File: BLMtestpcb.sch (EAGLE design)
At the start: 92 parts, among them IC1 NTB0102DP, IC10 PIC16F18325-I/P, IC11 MAX11644EUA+, IC4 PIC24F16KA301-I/SS,, IC5 NE555D, IC6 MULTIPLEX1, IC7 AD623R, IC8 AD822R, IC9 AD623R, Q3 12MHz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

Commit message: Update to V1.1
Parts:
- JP1: value Distance Select 0B -> Type select 0
- JP2: value Type Select 0 -> Setup select 0
- JP4: value Distance Select 0A -> Type select 0
- JP5: value Type Select 1 -> Setup select 1
- JP6: value Distance Select 1A -> Type select 1
- JP9: value Distance Select 1B -> Type select 1
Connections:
- net 0A_CLOSE renamed TYPE00A
- net 0B_FAR renamed TYPE01B
- net 1A_FAR renamed TYPE10A
- net 1B_FAR renamed TYPE11B
- net BPW34_2 renamed BOT1
- net N$1 renamed OP-AMP1
- net N$35 renamed OP-AMP0
- net SFH_2700 renamed TOP0
- removed net 0A_FAR: JP4.1, PHDA2.A
- removed net 0B_CLOSE: JP1.3, PHDB1.A
- removed net 1A_CLOSE: JP6.1, PHDA3.A
- removed net 1B_CLOSE: JP9.3, PHDB4.A
- removed net BPW34: JP2.3, JP4.2
- removed net SFH_2700_2: JP5.1, JP9.2
- new net BOT0: JP2.3, JP9.2
- new net TOP1: JP4.2, JP5.1
- new net TYPE00B: JP4.1, PHDB1.A
- new net TYPE01A: JP1.3, PHDA2.A
- new net TYPE10B: JP6.1, PHDB4.A
- new net TYPE11A: JP9.3, PHDA3.A
- net +3.3V: now also IC1.OE
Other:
- moved on the sheet: JP1, JP4, JP6, JP9, PHDA1, PHDA2, PHDA3, PHDA4, PHDB1, PHDB2, PHDB3, PHDB4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

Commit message: Update to v1.2
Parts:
- JP1, JP4: value Type select 0 -> Diode select 0
- JP13: value ADC select 0 -> ADC select
- JP14: value ADC select 1 -> ADC select
- JP2: value Setup select 0 -> Setup select
- JP20: value LED Select A -> LED Select 940
- JP21: value LED Select B -> LED Select 850
- JP22: value LED Select C -> LED Select 660
- JP5: value Setup select 1 -> Setup select
- JP6, JP9: value Type select 1 -> Diode select 1
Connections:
- net N$27 renamed 940A
- net N$28 renamed 940B
- net N$29 renamed 850A
- net N$30 renamed 850B
- net N$31 renamed 660A
- net N$32 renamed 660B
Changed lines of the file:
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@@
 <part name="R8" library="rcl" library_urn="urn:adsk.eagle:library:334" deviceset="R-EU_" device="0207/10" package3d_urn="urn:adsk.eagle:package:23491/2" value="180"/>
 <part name="R9" library="resistor" library_urn="urn:adsk.eagle:library:348" deviceset="R-EU_" device="0207/10" package3d_urn="urn:adsk.eagle:package:23491/2" value="150"/>
-<part name="JP20" library="pinhead" library_urn="urn:adsk.eagle:library:325" deviceset="PINHD-1X3" device="" package3d_urn="urn:adsk.eagle:package:22458/2" value="LED Select A"/>
-<part name="JP21" library="pinhead" library_urn="urn:adsk.eagle:library:325" deviceset="PINHD-1X3" device="" package3d_urn="urn:adsk.eagle:package:22458/2" value="LED Select B"/>
-<part name="JP22" library="pinhead" library_urn="urn:adsk.eagle:library:325" deviceset="PINHD-1X3" device="" package3d_urn="urn:adsk.eagle:package:22458/2" value="LED Select C"/>
+<part name="JP20" library="pinhead" library_urn="urn:adsk.eagle:library:325" deviceset="PINHD-1X3" device="" package3d_urn="urn:adsk.eagle:package:22458/2" value="LED Select 940"/>
+<part name="JP21" library="pinhead" library_urn="urn:adsk.eagle:library:325" deviceset="PINHD-1X3" device="" package3d_urn="urn:adsk.eagle:package:22458/2" value="LED Select 850"/>
+<part name="JP22" library="pinhead" library_urn="urn:adsk.eagle:library:325" deviceset="PINHD-1X3" device="" package3d_urn="urn:adsk.eagle:package:22458/2" value="LED Select 660"/>
 <part name="JP19" library="pinhead" library_urn="urn:adsk.eagle:library:325" deviceset="PINHD-1X3" device="" package3d_urn="urn:adsk.eagle:package:22458/2" value="Pwm Select"/>
 <part name="IC7" library="analog-devices" library_urn="urn:adsk.eagle:library:102" deviceset="AD623" device="R" package3d_urn="urn:adsk.eagle:package:30987/2"/>
@@
 <part name="GND" library="supply1" library_urn="urn:adsk.eagle:library:371" deviceset="GND" device=""/>
 <part name="JP12" library="pinhead" library_urn="urn:adsk.eagle:library:325" deviceset="PINHD-1X3" device="" package3d_urn="urn:adsk.eagle:package:22458/2" value="PWM Select"/>
-<part name="JP13" library="pinhead" library_urn="urn:adsk.eagle:library:325" deviceset="PINHD-1X3" device="" package3d_urn="urn:adsk.eagle:package:22458/2" value="ADC select 0"/>
-<part name="JP14" library="pinhead" library_urn="urn:adsk.eagle:library:325" deviceset="PINHD-1X3" device="" package3d_urn="urn:adsk.eagle:package:22458/2" value="ADC select 1"/>
+<part name="JP13" library="pinhead" library_urn="urn:adsk.eagle:library:325" deviceset="PINHD-1X3" device="" package3d_urn="urn:adsk.eagle:package:22458/2" value="ADC select"/>
+<part name="JP14" library="pinhead" library_urn="urn:adsk.eagle:library:325" deviceset="PINHD-1X3" device="" package3d_urn="urn:adsk.eagle:package:22458/2" value="ADC select"/>
 <part name="JP15" library="pinhead" library_urn="urn:adsk.eagle:library:325" deviceset="PINHD-1X3" device="" package3d_urn="urn:adsk.eagle:package:22458/2" value="MCU Select"/>
 <part name="JP16" library="pinhead" library_urn="urn:adsk.eagle:library:325" deviceset="PINHD-1X3" device="" package3d_urn="urn:adsk.eagle:package:22458/2" value="MCU Select"/>
@@
 <part name="PHDB4" library="adafruit" deviceset="DIODE" device="_SOD-123FL" value="SFH 2700"/>
 <part name="PHDA4" library="adafruit" deviceset="DIODE" device="SOT23_WAVE" value="BPW34"/>
-<part name="JP4" library="pinhead" library_urn="urn:adsk.eagle:library:325" deviceset="PINHD-1X3" device="" package3d_urn="urn:adsk.eagle:package:22458/2" value="Type select 0"/>
-<part name="JP1" library="pinhead" library_urn="urn:adsk.eagle:library:325" deviceset="PINHD-1X3" device="" package3d_urn="urn:adsk.eagle:package:22458/2" value="Type select 0"/>
-<part name="JP2" library="pinhead" library_urn="urn:adsk.eagle:library:325" deviceset="PINHD-1X3" device="" package3d_urn="urn:adsk.eagle:package:22458/2" value="Setup select 0"/>
-<part name="JP5" library="pinhead" library_urn="urn:adsk.eagle:library:325" deviceset="PINHD-1X3" device="" package3d_urn="urn:adsk.eagle:package:22458/2" value="Setup select 1"/>
-<part name="JP6" library="pinhead" library_urn="urn:adsk.eagle:library:325" deviceset="PINHD-1X3" device="" package3d_urn="urn:adsk.eagle:package:22458/2" value="Type select 1"/>
-<part name="JP9" library="pinhead" library_urn="urn:adsk.eagle:library:325" deviceset="PINHD-1X3" device="" package3d_urn="urn:adsk.eagle:package:22458/2" value="Type select 1"/>
+<part name="JP4" library="pinhead" library_urn="urn:adsk.eagle:library:325" deviceset="PINHD-1X3" device="" package3d_urn="urn:adsk.eagle:package:22458/2" value="Diode select 0"/>
+<part name="JP1" library="pinhead" library_urn="urn:adsk.eagle:library:325" deviceset="PINHD-1X3" device="" package3d_urn="urn:adsk.eagle:package:22458/2" value="Diode select 0"/>
+<part name="JP2" library="pinhead" library_urn="urn:adsk.eagle:library:325" deviceset="PINHD-1X3" device="" package3d_urn="urn:adsk.eagle:package:22458/2" value="Setup select"/>
+<part name="JP5" library="pinhead" library_urn="urn:adsk.eagle:library:325" deviceset="PINHD-1X3" device="" package3d_urn="urn:adsk.eagle:package:22458/2" value="Setup select"/>
+<part name="JP6" library="pinhead" library_urn="urn:adsk.eagle:library:325" deviceset="PINHD-1X3" device="" package3d_urn="urn:adsk.eagle:package:22458/2" value="Diode select 1"/>
+<part name="JP9" library="pinhead" library_urn="urn:adsk.eagle:library:325" deviceset="PINHD-1X3" device="" package3d_urn="urn:adsk.eagle:package:22458/2" value="Diode select 1"/>
 <part name="JP10" library="pinhead" library_urn="urn:adsk.eagle:library:325" deviceset="PINHD-1X6" device="" package3d_urn="urn:adsk.eagle:package:22472/2" value="PIC24F16 header"/>
 <part name="JP17" library="pinhead" library_urn="urn:adsk.eagle:library:325" deviceset="PINHD-1X6" device="" package3d_urn="urn:adsk.eagle:package:22472/2" value="PIC16F18 header"/>
@@
 </segment>
 </net>
-<net name="N$27" class="0">
+<net name="940A" class="0">
 <segment>
 <pinref part="R4" gate="G$1" pin="2"/>
@@
 </segment>
 </net>
-<net name="N$28" class="0">
+<net name="940B" class="0">
 <segment>
 <pinref part="JP20" gate="A" pin="1"/>
@@
 </segment>
 </net>
-<net name="N$29" class="0">
+<net name="850A" class="0">
 <segment>
 <pinref part="R5" gate="G$1" pin="2"/>
@@
 </segment>
 </net>
-<net name="N$30" class="0">
+<net name="850B" class="0">
 <segment>
 <pinref part="JP21" gate="A" pin="1"/>
@@
 </segment>
 </net>
-<net name="N$31" class="0">
+<net name="660A" class="0">
 <segment>
 <pinref part="R6" gate="G$1" pin="2"/>
@@
 </segment>
 </net>
-<net name="N$32" class="0">
+<net name="660B" class="0">
 <segment>
 <pinref part="JP22" gate="A" pin="1"/>

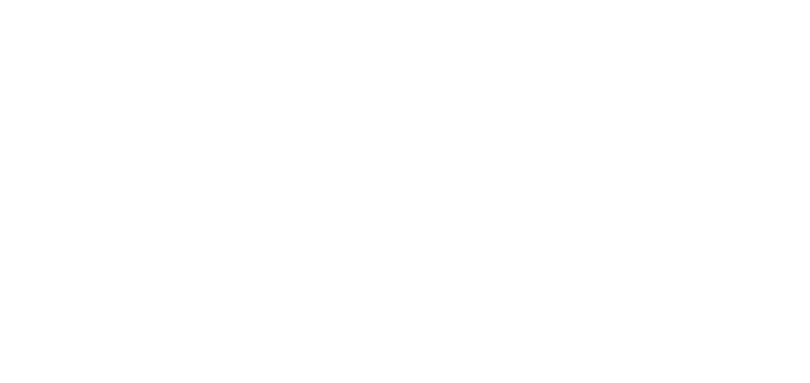
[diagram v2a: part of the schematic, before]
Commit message: Update to v1_3
Change some component footprints to have pin 1 indication. Remove 1mm length difference in PCB
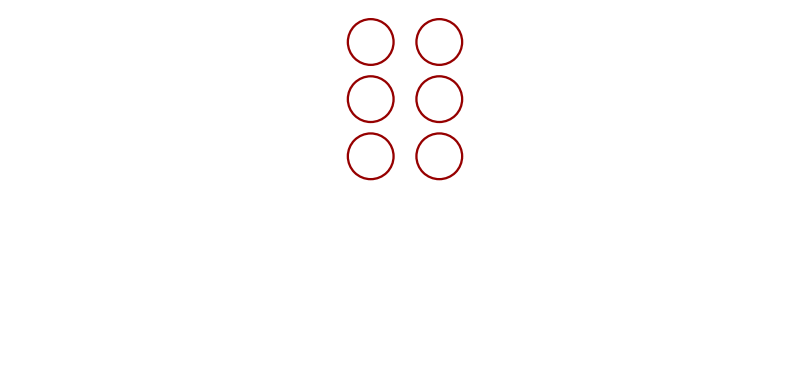
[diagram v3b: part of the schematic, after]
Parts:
- added U$1, U$2, U$3, U$4, U$5, U$6: FIDUCIAL, adafruit:FIDUCIAL
- IC5: device linear:NE555D -> linear_custom:NE555D
- IC7, IC9: device analog-devices:AD623R -> analog-devices_custom:AD623R
- IC8: device analog-devices:AD822R -> analog-devices_custom:AD822R
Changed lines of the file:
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@@
 <?xml version="1.0" encoding="utf-8"?>
 <!DOCTYPE eagle SYSTEM "eagle.dtd">
-<eagle version="9.5.1">
+<eagle version="9.4.2">
 <drawing>
 <settings>
@@
 </classes>
 <parts>
-<part name="IC5" library="linear" library_urn="urn:adsk.eagle:library:262" deviceset="*555" device="D" package3d_urn="urn:adsk.eagle:package:16404/2" technology="NE"/>
+<part name="IC5" library="linear_custom" deviceset="*555" device="D" package3d_urn="urn:adsk.eagle:package:16404/2" technology="NE"/>
 <part name="IC6" library="Peerke" deviceset="MULTIPLEX1" device=""/>
 <part name="LED1" library="adafruit" deviceset="LED" device="CHIPLED_1206" value="1328301"/>
@@
 <part name="JP22" library="pinhead" library_urn="urn:adsk.eagle:library:325" deviceset="PINHD-1X3" device="" package3d_urn="urn:adsk.eagle:package:22458/2" value="LED Select 660"/>
 <part name="JP19" library="pinhead" library_urn="urn:adsk.eagle:library:325" deviceset="PINHD-1X3" device="" package3d_urn="urn:adsk.eagle:package:22458/2" value="Pwm Select"/>
-<part name="IC7" library="analog-devices" library_urn="urn:adsk.eagle:library:102" deviceset="AD623" device="R" package3d_urn="urn:adsk.eagle:package:30987/2"/>
-<part name="IC8" library="analog-devices" library_urn="urn:adsk.eagle:library:102" deviceset="AD822" device="R" package3d_urn="urn:adsk.eagle:package:30987/2"/>
+<part name="IC7" library="analog-devices_custom" deviceset="AD623" device="R" package3d_urn="urn:adsk.eagle:package:30987/2"/>
+<part name="IC8" library="analog-devices_custom" deviceset="AD822" device="R" package3d_urn="urn:adsk.eagle:package:30987/2"/>
 <part name="GND7" library="supply1" deviceset="GND" device=""/>
 <part name="GND8" library="supply1" deviceset="GND" device=""/>
@@
 <part name="GND12" library="supply1" deviceset="GND" device=""/>
 <part name="POTMETER2" library="pot" library_urn="urn:adsk.eagle:library:331" deviceset="TRIM_EU-" device="PT10" package3d_urn="urn:adsk.eagle:package:22715/1" value="10k-100k"/>
-<part name="IC9" library="analog-devices" library_urn="urn:adsk.eagle:library:102" deviceset="AD623" device="R" package3d_urn="urn:adsk.eagle:package:30987/2"/>
+<part name="IC9" library="analog-devices_custom" deviceset="AD623" device="R" package3d_urn="urn:adsk.eagle:package:30987/2"/>
 <part name="R13" library="rcl" library_urn="urn:adsk.eagle:library:334" deviceset="R-EU_" device="0207/10" value="100k"/>
 <part name="R14" library="rcl" library_urn="urn:adsk.eagle:library:334" deviceset="R-EU_" device="0207/10" package3d_urn="urn:adsk.eagle:package:23491/2" value="1M"/>
@@
 <part name="GND15" library="supply1" library_urn="urn:adsk.eagle:library:371" deviceset="GND" device=""/>
 <part name="C16" library="rcl" library_urn="urn:adsk.eagle:library:334" deviceset="C-EU" device="025-024X044" package3d_urn="urn:adsk.eagle:package:23630/1" value="100n"/>
+<part name="U$1" library="adafruit" deviceset="FIDUCIAL" device=""/>
+<part name="U$2" library="adafruit" deviceset="FIDUCIAL" device=""/>
+<part name="U$3" library="adafruit" deviceset="FIDUCIAL" device=""/>
+<part name="U$4" library="adafruit" deviceset="FIDUCIAL" device=""/>
+<part name="U$5" library="adafruit" deviceset="FIDUCIAL" device=""/>
+<part name="U$6" library="adafruit" deviceset="FIDUCIAL" device=""/>
 </parts>
 <sheets>
@@
 <attribute name="VALUE" x="340.614" y="56.261" size="1.778" layer="96"/>
 </instance>
+<instance part="U$1" gate="G$1" x="113.03" y="172.72" smashed="yes"/>
+<instance part="U$2" gate="G$1" x="113.03" y="166.37" smashed="yes"/>
+<instance part="U$3" gate="G$1" x="113.03" y="160.02" smashed="yes"/>
+<instance part="U$4" gate="G$1" x="120.65" y="172.72" smashed="yes"/>
+<instance part="U$5" gate="G$1" x="120.65" y="166.37" smashed="yes"/>
+<instance part="U$6" gate="G$1" x="120.65" y="160.02" smashed="yes"/>
 </instances>
 <busses>
